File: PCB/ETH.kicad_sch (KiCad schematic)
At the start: 33 parts, among them J6 RJ45_Pulse_JXD6-0001NL, U6 DP83848C, Y2 50M

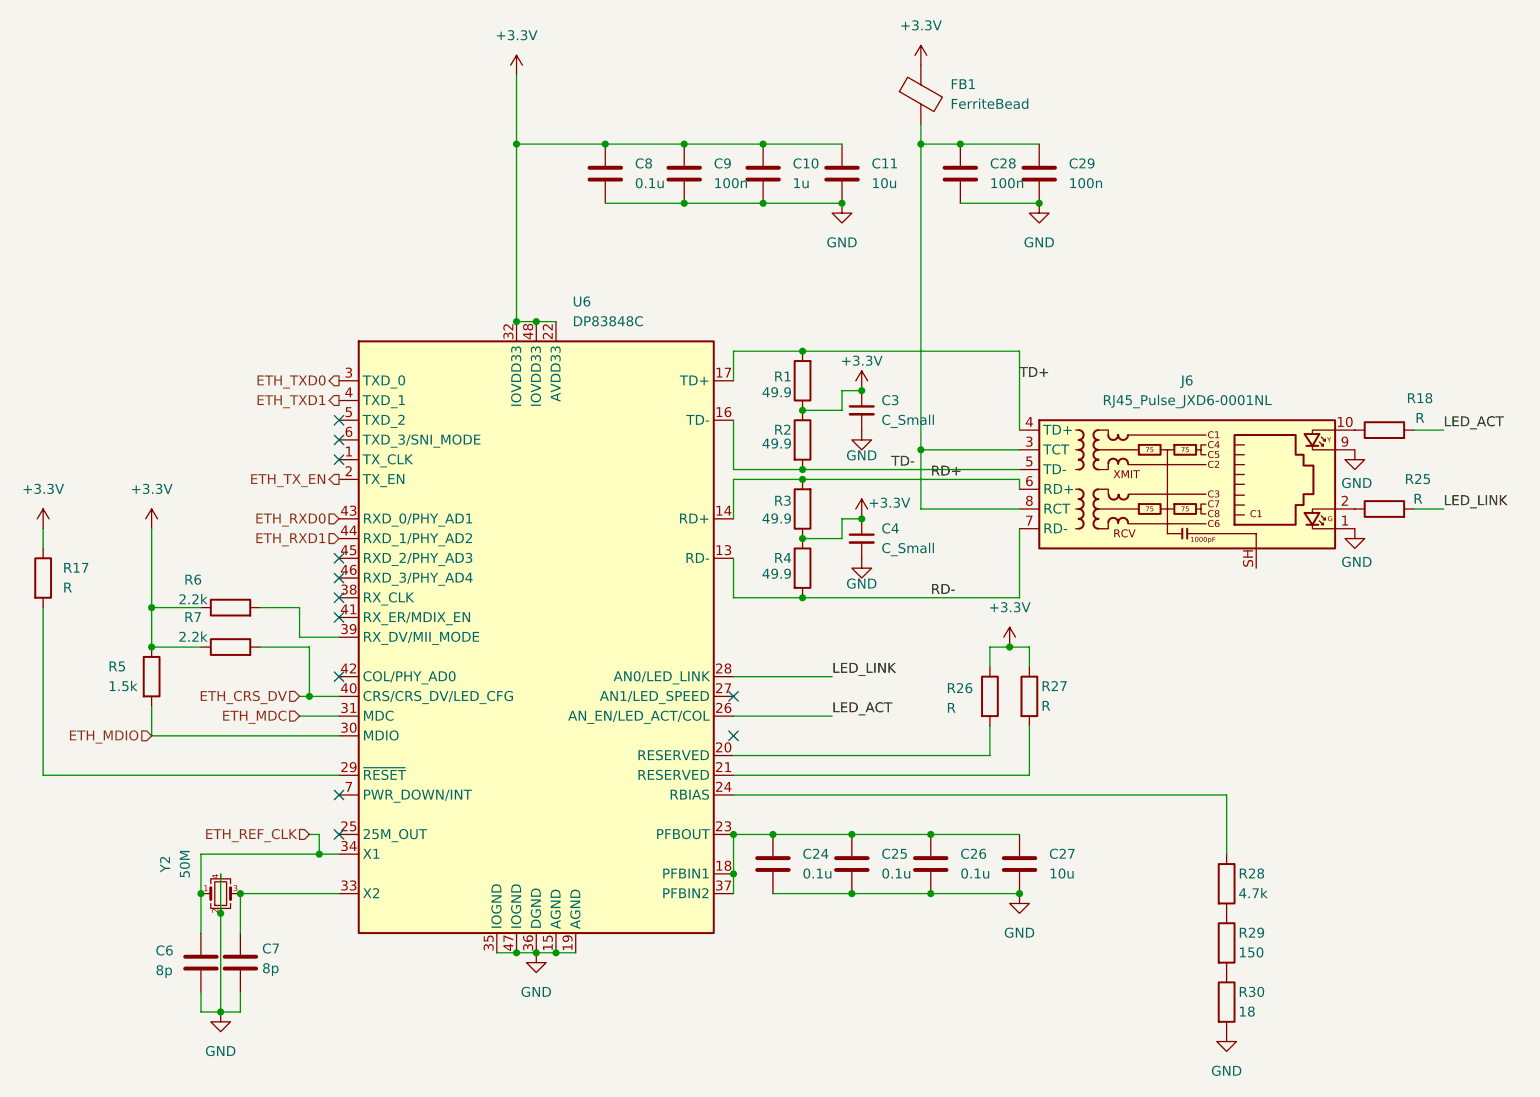
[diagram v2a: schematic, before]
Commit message: update:基板発注した
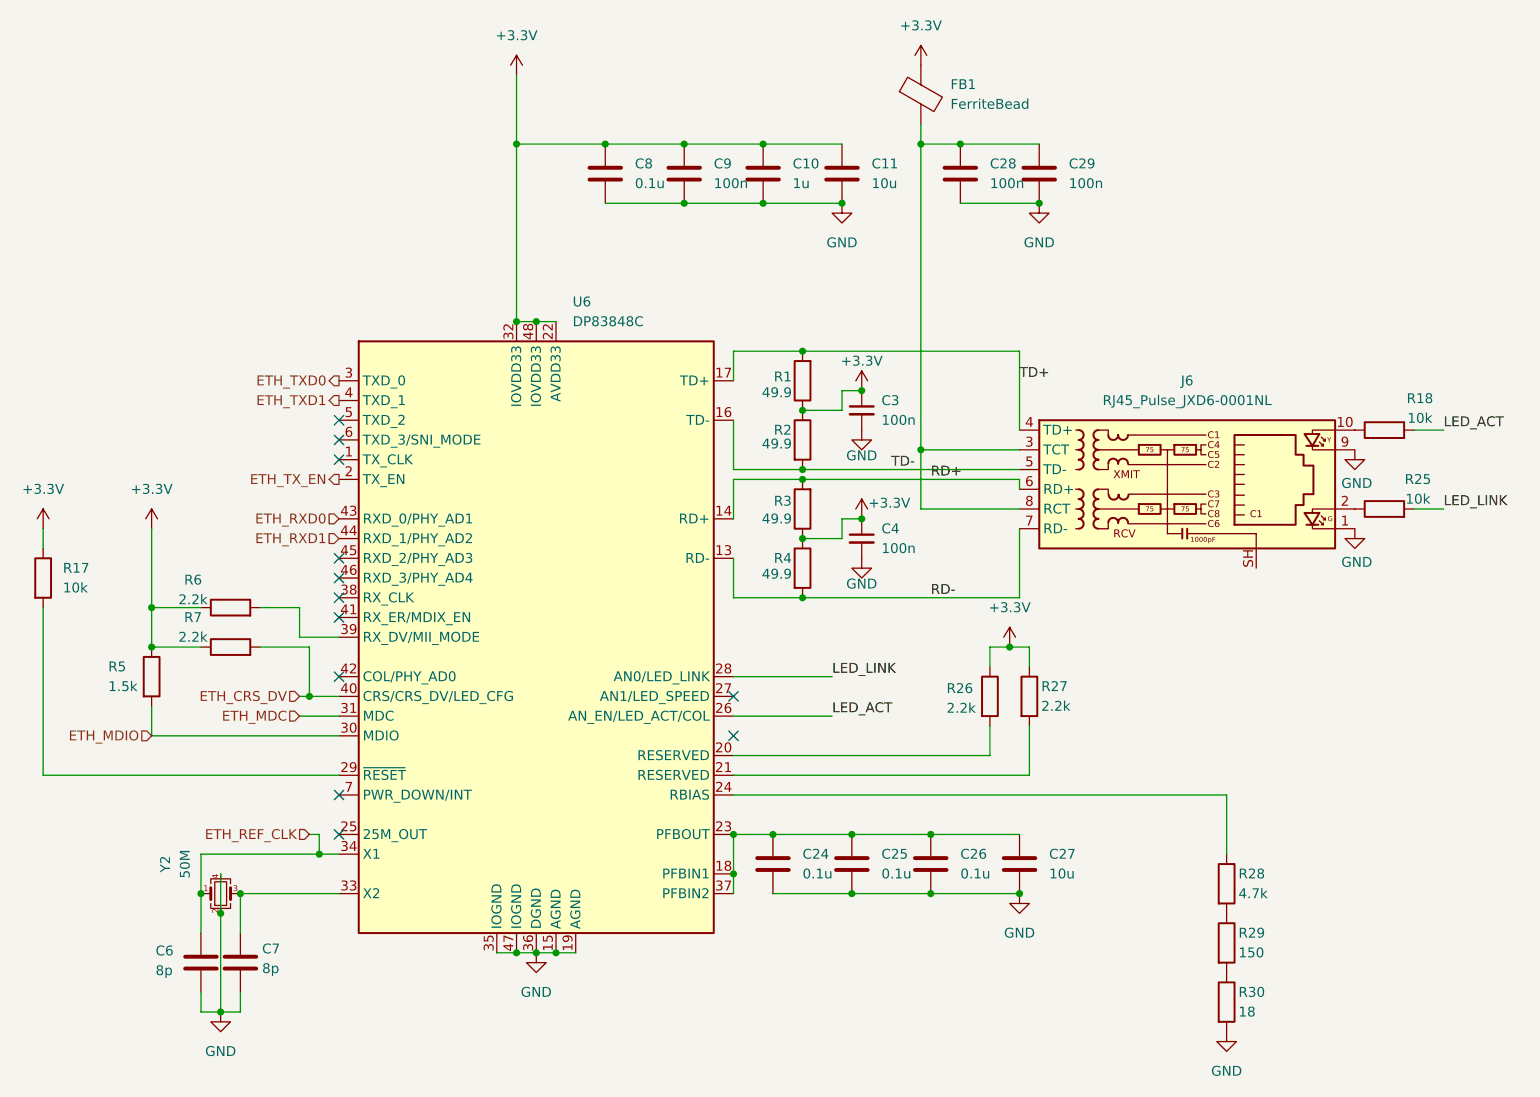
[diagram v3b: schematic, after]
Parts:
- C3, C4: value C_Small -> 100n
- R17, R18, R25: value R -> 10k
- R26, R27: value R -> 2.2k
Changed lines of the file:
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@@
 			)
 		)
-		(property "Value" "R"
+		(property "Value" "2.2k"
 			(at 192.532 114.554 0)
 			(effects
@@
 			)
 		)
-		(property "Value" "R"
+		(property "Value" "10k"
 			(at 253.492 77.216 90)
 			(effects
@@
 			)
 		)
-		(property "Value" "R"
+		(property "Value" "2.2k"
 			(at 204.724 114.3 0)
 			(effects
@@
 			)
 		)
-		(property "Value" "R"
+		(property "Value" "10k"
 			(at 78.74 99.0599 0)
 			(effects
@@
 			)
 		)
-		(property "Value" "R"
+		(property "Value" "10k"
 			(at 253.238 87.63 90)
 			(effects
@@
 			)
 		)
-		(property "Value" "C_Small"
+		(property "Value" "100n"
 			(at 184.15 77.4762 0)
 			(effects
@@
 			)
 		)
-		(property "Value" "C_Small"
+		(property "Value" "100n"
 			(at 184.15 93.9862 0)
 			(effects
